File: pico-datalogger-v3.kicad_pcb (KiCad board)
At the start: 2 copper layers, 130 x 65 mm, 59 parts, among them IC1 LM66200DRLR, J1 JST-PH2 Bat, J11 Conn_I2C1, J12 Conn_UART_5V, J13 THT_I2C1, J14 THT_I2C0, J17 Disp_THT, J2 Conn_Pico_Left, J3 Conn_Pico_Right, J4 SM06B-GHS-TB_LF_SN, J6 Conn_Display, J9 Conn_I2C0, Q1 AO3401A, Q2 AO3401A, SW1 SW_Push, SW2 SW_Push, SW3 SW_Push, SW4 SW_Push, SW5 SW_Push, U1 74LVC2G74, U2 PCF8523T, U4 XTSD, U5 SCD40_Breakout, U6 AHT20, U7 RFM95W-868S2, Y1 Crystal

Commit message: fix pin-order for SEN66-connector
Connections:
- J2 pad 20: Lora_EN -> Lora_DIO0
- J4 pad 1: unconnected-(J4-Pad1) -> +3V3
- J4 pad 2: unconnected-(J4-Pad2) -> GND
- J4 pad 3: unconnected-(J4-Pad3) -> SCL
- J4 pad 4: unconnected-(J4-Pad4) -> SDA
- J4 pad 5: unconnected-(J4-Pad5) -> GND
- J4 pad 6: unconnected-(J4-Pad6) -> +3V3

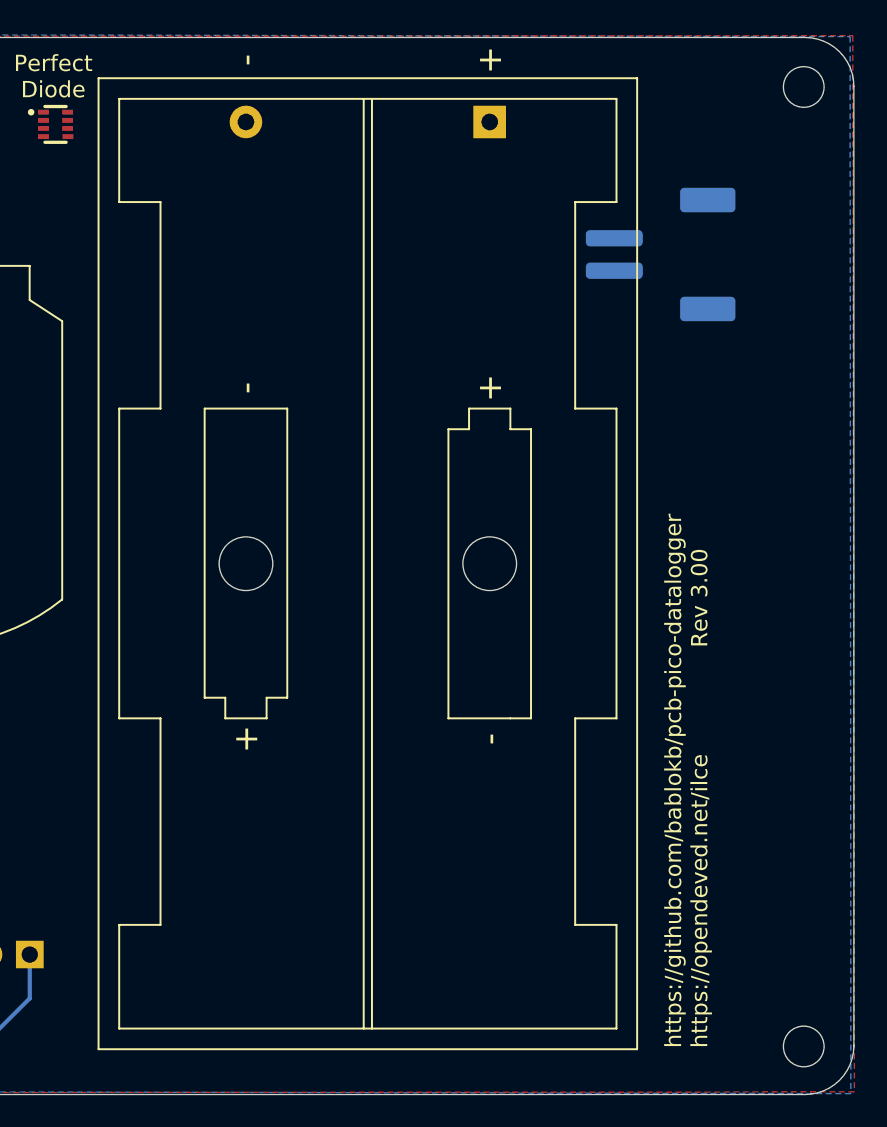
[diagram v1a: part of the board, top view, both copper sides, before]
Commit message: switch to user:JST-PH2
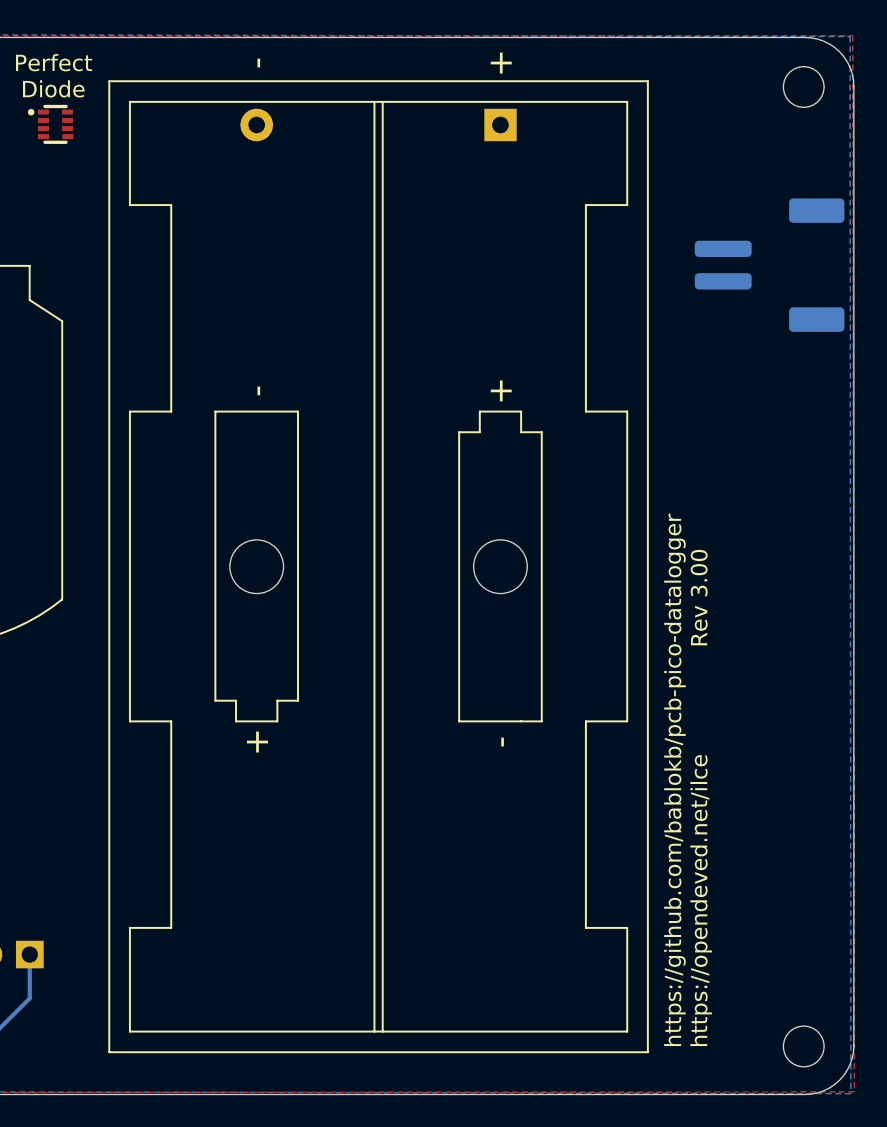
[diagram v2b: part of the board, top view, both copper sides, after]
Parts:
- J1: footprint Connector_JST:JST_PH_S2B-PH-SM4-TB_1x02-1MP_P2.00mm_Horizontal -> user:JST_PH_S2B-PH-SM4-TB_1x02-1MP_P2.00mm_Horizontal
- moved J1 6.73 mm to (224.9, 114.0)
- moved BT2 0.69 mm to (208.3, 105.3)
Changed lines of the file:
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@@
   )
   (footprint "Battery:BatteryHolder_Keystone_2462_2xAA" (layer "F.Cu")
-    (at 207.69 105.15 -90)
+    (at 208.35 105.335 -90)
     (descr "2xAA cell battery holder, Keystone P/N 2462, https://www.keyelco.com/product-pdf.cfm?p=1027")
     (tags "AA battery cell holder")
@@
     )
   )
-  (footprint "Connector_JST:JST_PH_S2B-PH-SM4-TB_1x02-1MP_P2.00mm_Horizontal" (layer "B.Cu")
-    (at 218.2 113.3 -90)
+  (footprint "user:JST_PH_S2B-PH-SM4-TB_1x02-1MP_P2.00mm_Horizontal" (layer "B.Cu")
+    (at 224.9 113.95 -90)
     (descr "JST PH series connector, S2B-PH-SM4-TB (http://www.jst-mfg.com/product/pdf/eng/ePH.pdf), generated with kicad-footprint-generator")
     (tags "connector JST PH top entry")
@@
     (pad "2" smd roundrect (at 1 2.85 270) (size 1 3.5) (layers "B.Cu" "B.Paste" "B.Mask") (roundrect_rratio 0.25)
       (net 2 "GND") (pinfunction "Pin_2") (pintype "passive"))
-    (pad "MP" smd roundrect (at -3.35 -2.9 270) (size 1.5 3.4) (layers "B.Cu" "B.Paste" "B.Mask") (roundrect_rratio 0.1666673333))
-    (pad "MP" smd roundrect (at 3.35 -2.9 270) (size 1.5 3.4) (layers "B.Cu" "B.Paste" "B.Mask") (roundrect_rratio 0.1666673333))
+    (pad "MP" smd roundrect (at -3.35 -2.9 270) (size 1.5 3.4) (layers "B.Cu" "B.Paste" "B.Mask") (roundrect_rratio 0.166667))
+    (pad "MP" smd roundrect (at 3.35 -2.9 270) (size 1.5 3.4) (layers "B.Cu" "B.Paste" "B.Mask") (roundrect_rratio 0.166667))
     (model "${KICAD6_3DMODEL_DIR}/Connector_JST.3dshapes/JST_PH_S2B-PH-SM4-TB_1x02-1MP_P2.00mm_Horizontal.wrl"
       (offset (xyz 0 0 0))
@@
       (rotate (xyz 0 0 0))
     )
-    (model "/home/bablokb/kicad/S2B-PH-SM4-TB.step"
+    (model "/home/bablokb/kicad7/3dmodules/user.3dshapes/S2B-PH-SM4-TB.step"
       (offset (xyz 0 -4.5 -0.1))
       (scale (xyz 1 1 1))
@@
     (effects (font (size 0.9 0.9) (thickness 0.15)) (justify mirror))
   )
-  (gr_text "+" (at 212.25 112.3 -90) (layer "B.SilkS")
+  (gr_text "+" (at 219.25 113 -90) (layer "B.SilkS")
     (effects (font (size 1 1) (thickness 0.15)) (justify mirror))
   )
@@
     (effects (font (size 0.9 0.9) (thickness 0.15)) (justify mirror))
   )
-  (gr_text "AA-Bat/LiPo" (at 218.85 108) (layer "B.SilkS")
+  (gr_text "AA-Bat/LiPo" (at 224.85 108.65) (layer "B.SilkS")
     (effects (font (size 0.9 0.9) (thickness 0.15)) (justify mirror))
   )
@@
     (effects (font (size 0.9 0.9) (thickness 0.15)) (justify mirror))
   )
-  (gr_text "-" (at 212.2 114.35 -90) (layer "B.SilkS")
+  (gr_text "-" (at 219.3 114.9 -90) (layer "B.SilkS")
     (effects (font (size 1 1) (thickness 0.15)) (justify mirror))
   )

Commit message: switch to user:JST-SH4
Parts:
- J11, J9: footprint Connector_JST:JST_SH_SM04B-SRSS-TB_1x04-1MP_P1.00mm_Horizontal -> user:JST_SH_SM04B-SRSS-TB_1x04-1MP_P1.00mm_Horizontal
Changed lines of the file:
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@@
       (stroke (width 0) (type solid)) (fill solid) (layer "B.SilkS"))
   )
-  (footprint "Connector_JST:JST_SH_SM04B-SRSS-TB_1x04-1MP_P1.00mm_Horizontal" (layer "B.Cu")
+  (footprint "user:JST_SH_SM04B-SRSS-TB_1x04-1MP_P1.00mm_Horizontal" (layer "B.Cu")
     (at 148.54 102.95)
     (descr "JST SH series connector, SM04B-SRSS-TB (http://www.jst-mfg.com/product/pdf/eng/eSH.pdf), generated with kicad-footprint-generator")
@@
     (property "ki_keywords" "connector")
     (attr smd)
-    (fp_text reference "J9" (at 0 3.98) (layer "B.SilkS") hide
-        (effects (font (size 1 1) (thickness 0.15)) (justify mirror))
-    )
-    (fp_text value "Conn_I2C0" (at 0 -3.98) (layer "B.Fab") hide
-        (effects (font (size 1 1) (thickness 0.15)) (justify mirror))
-    )
-    (fp_text user "${REFERENCE}" (at 0 0) (layer "B.Fab") hide
+    (fp_text reference "J9" (at 0 3.98 180) (layer "B.SilkS") hide
+        (effects (font (size 1 1) (thickness 0.15)) (justify mirror))
+    )
+    (fp_text value "Conn_I2C0" (at 0 -3.98 180) (layer "B.Fab")
+        (effects (font (size 1 1) (thickness 0.15)) (justify mirror))
+    )
+    (fp_text user "${REFERENCE}" (at 0 0 180) (layer "B.Fab")
         (effects (font (size 1 1) (thickness 0.15)) (justify mirror))
     )
@@
     (pad "4" smd roundrect (at 1.5 2) (size 0.6 1.55) (layers "B.Cu" "B.Paste" "B.Mask") (roundrect_rratio 0.25)
       (net 13 "/RX") (pinfunction "SCL") (pintype "bidirectional"))
-    (pad "MP" smd roundrect (at -2.8 -1.875) (size 1.2 1.8) (layers "B.Cu" "B.Paste" "B.Mask") (roundrect_rratio 0.2083333333))
-    (pad "MP" smd roundrect (at 2.8 -1.875) (size 1.2 1.8) (layers "B.Cu" "B.Paste" "B.Mask") (roundrect_rratio 0.2083333333))
+    (pad "MP" smd roundrect (at -2.8 -1.875) (size 1.2 1.8) (layers "B.Cu" "B.Paste" "B.Mask") (roundrect_rratio 0.208333))
+    (pad "MP" smd roundrect (at 2.8 -1.875) (size 1.2 1.8) (layers "B.Cu" "B.Paste" "B.Mask") (roundrect_rratio 0.208333))
     (model "${KICAD6_3DMODEL_DIR}/Connector_JST.3dshapes/JST_SH_SM04B-SRSS-TB_1x04-1MP_P1.00mm_Horizontal.wrl"
       (offset (xyz 0 0 0))
@@
       (rotate (xyz 0 0 0))
     )
-    (model "/home/bablokb/kicad/SM04B-SRSS-TB.step"
+    (model "/home/bablokb/kicad7/SM04B-SRSS-TB.step"
       (offset (xyz 0 1.35 -0.35))
       (scale (xyz 1 1 1))
@@
     )
   )
-  (footprint "Connector_JST:JST_SH_SM04B-SRSS-TB_1x04-1MP_P1.00mm_Horizontal" (layer "B.Cu")
+  (footprint "user:JST_SH_SM04B-SRSS-TB_1x04-1MP_P1.00mm_Horizontal" (layer "B.Cu")
     (at 133.65 103.55)
     (descr "JST SH series connector, SM04B-SRSS-TB (http://www.jst-mfg.com/product/pdf/eng/eSH.pdf), generated with kicad-footprint-generator")
@@
     (property "ki_keywords" "connector")
     (attr smd)
-    (fp_text reference "J11" (at 0 3.98) (layer "B.SilkS") hide
-        (effects (font (size 1 1) (thickness 0.15)) (justify mirror))
-    )
-    (fp_text value "Conn_I2C1" (at 0 -3.98) (layer "B.Fab") hide
-        (effects (font (size 1 1) (thickness 0.15)) (justify mirror))
-    )
-    (fp_text user "${REFERENCE}" (at 0 0) (layer "B.Fab") hide
+    (fp_text reference "J11" (at 0 3.98 180) (layer "B.SilkS") hide
+        (effects (font (size 1 1) (thickness 0.15)) (justify mirror))
+    )
+    (fp_text value "Conn_I2C1" (at 0 -3.98 180) (layer "B.Fab")
+        (effects (font (size 1 1) (thickness 0.15)) (justify mirror))
+    )
+    (fp_text user "${REFERENCE}" (at 0 0 180) (layer "B.Fab")
         (effects (font (size 1 1) (thickness 0.15)) (justify mirror))
     )
@@
     (pad "4" smd roundrect (at 1.5 2) (size 0.6 1.55) (layers "B.Cu" "B.Paste" "B.Mask") (roundrect_rratio 0.25)
       (net 15 "SCL") (pinfunction "SCL") (pintype "bidirectional"))
-    (pad "MP" smd roundrect (at -2.8 -1.875) (size 1.2 1.8) (layers "B.Cu" "B.Paste" "B.Mask") (roundrect_rratio 0.2083333333))
-    (pad "MP" smd roundrect (at 2.8 -1.875) (size 1.2 1.8) (layers "B.Cu" "B.Paste" "B.Mask") (roundrect_rratio 0.2083333333))
+    (pad "MP" smd roundrect (at -2.8 -1.875) (size 1.2 1.8) (layers "B.Cu" "B.Paste" "B.Mask") (roundrect_rratio 0.208333))
+    (pad "MP" smd roundrect (at 2.8 -1.875) (size 1.2 1.8) (layers "B.Cu" "B.Paste" "B.Mask") (roundrect_rratio 0.208333))
     (model "${KICAD6_3DMODEL_DIR}/Connector_JST.3dshapes/JST_SH_SM04B-SRSS-TB_1x04-1MP_P1.00mm_Horizontal.wrl"
       (offset (xyz 0 0 0))
@@
       (rotate (xyz 0 0 0))
     )
-    (model "/home/bablokb/kicad/SM04B-SRSS-TB.step"
+    (model "/home/bablokb/kicad7/SM04B-SRSS-TB.step"
       (offset (xyz 0 1.35 -0.35))
       (scale (xyz 1 1 1))
@@
     (effects (font (size 1 1) (thickness 0.15)) (justify left bottom mirror))
   )
-  (gr_text "3V3" (at 149.58 106.56) (layer "B.SilkS")
-    (effects (font (size 0.8 0.8) (thickness 0.15)) (justify mirror))
-  )
   (gr_text "Reset" (at 156.1 153.5) (layer "B.SilkS")
     (effects (font (size 1 1) (thickness 0.15)) (justify left bottom mirror))
@@
     (effects (font (size 0.9 0.9) (thickness 0.15)) (justify mirror))
   )
-  (gr_text "RX" (at 144.5 106.56) (layer "B.SilkS")
-    (effects (font (size 0.8 0.8) (thickness 0.15)) (justify mirror))
-  )
-  (gr_text "TX" (at 147.07 106.59) (layer "B.SilkS")
-    (effects (font (size 0.8 0.8) (thickness 0.15)) (justify mirror))
-  )
   (gr_text "I2C0" (at 143.95 105.38) (layer "B.SilkS")
     (effects (font (size 0.9 0.9) (thickness 0.15)) (justify mirror))
@@
     (effects (font (size 1 1) (thickness 0.15)) (justify left bottom mirror))
   )
-  (gr_text "GND" (at 152.21 106.48) (layer "B.SilkS")
-    (effects (font (size 0.8 0.8) (thickness 0.15)) (justify mirror))
-  )
   (gr_text "GND" (at 152.411906 134.65) (layer "B.SilkS")

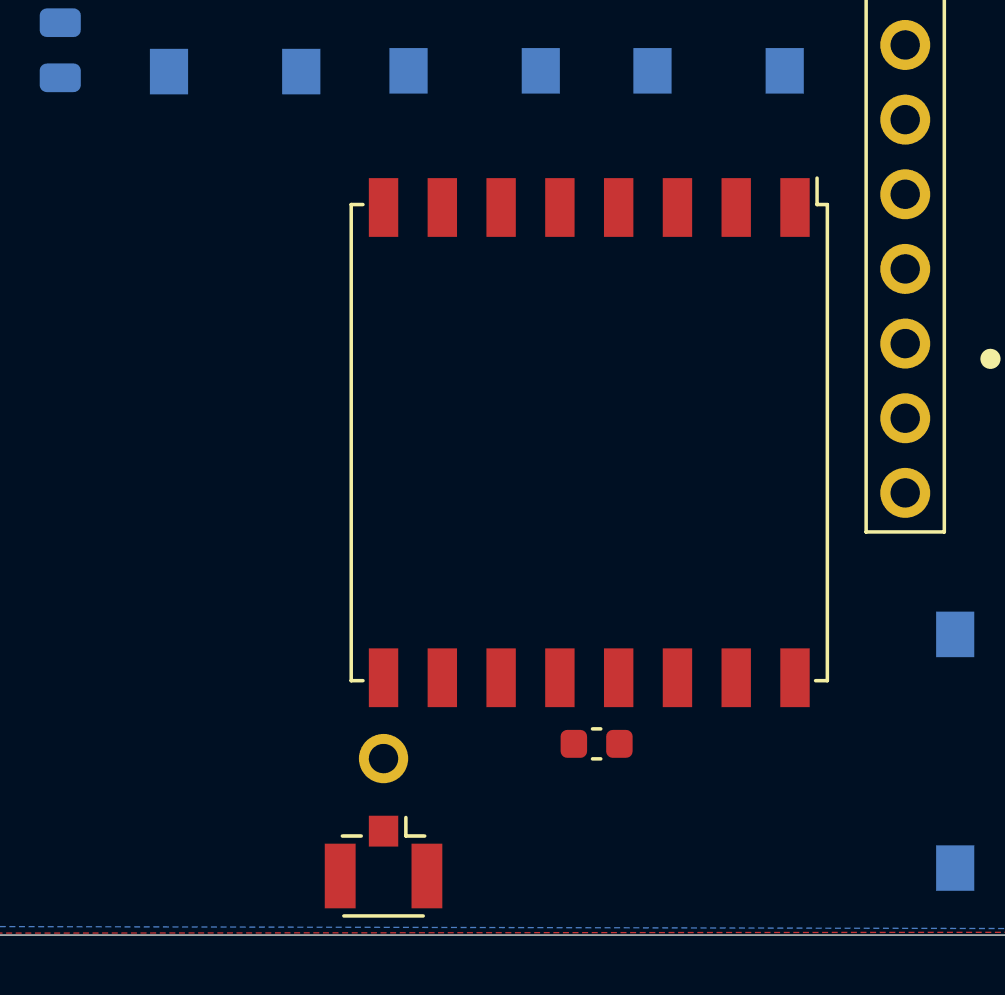
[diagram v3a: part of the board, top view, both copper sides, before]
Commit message: update footprint RFM96x
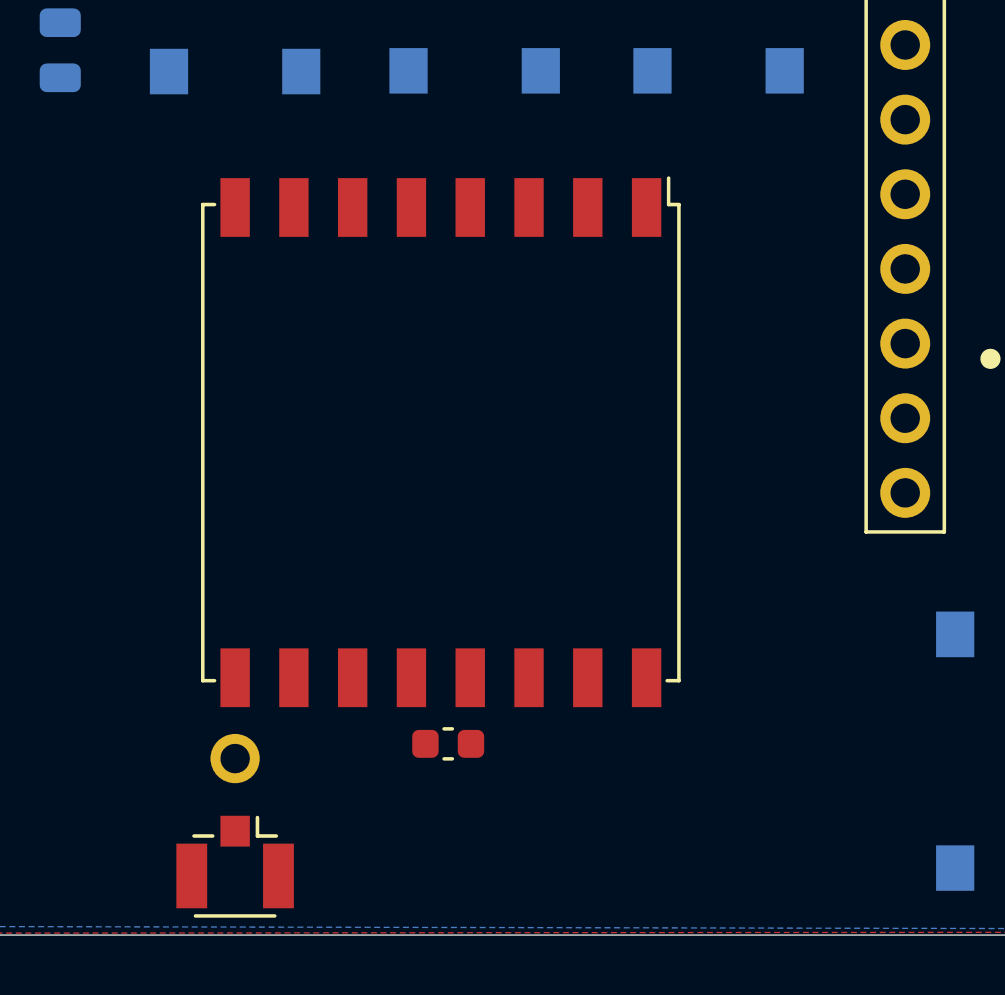
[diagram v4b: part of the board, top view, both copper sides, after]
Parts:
- moved AE1 5.05 mm to (116.8, 162.2)
- moved AE2 5.05 mm to (116.8, 158.9)
- moved C6 5.05 mm to (124.1, 158.4)
- moved U7 5.05 mm to (123.8, 148.2)
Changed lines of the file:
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@@
   )
   (footprint "user:Antenna_THT" (layer "F.Cu")
-    (at 121.9 158.95)
+    (at 116.85 158.95)
     (descr "Antenna connector THT")
     (tags "Antenna, THT")
@@
   )
   (footprint "user:U.FL_Hirose_U.FL-R-SMT-1_Vertical" (layer "F.Cu")
-    (at 121.9 162.226 -90)
+    (at 116.85 162.226 -90)
     (descr "Hirose U.FL Coaxial https://www.hirose.com/product/en/products/U.FL/U.FL-R-SMT-1%2810%29/")
     (tags "Hirose U.FL Coaxial")
@@
   )
   (footprint "Capacitor_SMD:C_0603_1608Metric" (layer "F.Cu")
-    (at 129.15 158.45)
+    (at 124.1 158.45)
     (descr "Capacitor SMD 0603 (1608 Metric), square (rectangular) end terminal, IPC_7351 nominal, (Body size source: IPC-SM-782 page 76, https://www.pcb-3d.com/wordpress/wp-content/uploads/ipc-sm-782a_amendment_1_and_2.pdf), generated with kicad-footprint-generator")
     (tags "capacitor")
@@
   )
   (footprint "user:HOPERF_RFM9XW_SMD" (layer "F.Cu")
-    (at 128.9 148.2 -90)
+    (at 123.85 148.2 -90)
     (descr "Low Power Long Range Transceiver Module SMD-16 (https://www.hoperf.com/data/upload/portal/20181127/5bfcbea20e9ef.pdf)")
     (tags "LoRa Low Power Long Range Transceiver Module")
@@
     (pad "16" smd rect (at 8 -7 270) (size 2 1) (layers "F.Cu" "F.Paste" "F.Mask")
       (net 61 "unconnected-(U7-DIO2-Pad16)") (pinfunction "DIO2") (pintype "bidirectional+no_connect"))
-    (model "${KICAD6_3DMODEL_DIR}/RF_Module.3dshapes/HOPERF_RFM9XW_SMD.wrl"
-      (offset (xyz 0 0 0))
-      (scale (xyz 1 1 1))
-      (rotate (xyz 0 0 0))
-    )
-    (model "/home/bablokb/kicad/RFM95W.STEP"
-      (offset (xyz 0 0 0))
-      (scale (xyz 1 1 1))
+    (model "/home/bablokb/kicad7/3dmodules/user.3dshapes/RFM95W.step"
+      (offset (xyz 0 0 0))
+      (scale (xyz 1 1 1))
